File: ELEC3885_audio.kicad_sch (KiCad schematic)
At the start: 27 parts, among them U2 SGTL5000XNLA3, U3 AP7313

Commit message: Schematic work
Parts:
- removed J?: LineOutL, symbol Connector:AudioJack2
- removed J?: LineOutR, symbol Connector:AudioJack2
- removed J?: LineIn, symbol Connector:AudioJack3
- removed L1: Ferrite 600, symbol Device:L
- added C7: 1uF, Capacitor_SMD:C_0402_1005Metric, symbol Device:C_Small
- added FB1: FerriteBead, Inductor_SMD:L_0603_1608Metric, symbol Device:FerriteBead
- added J2: LineIn, Connector_Audio:Jack_3.5mm_CUI_SJ1-3535NG_Horizontal, symbol Connector:AudioJack3_SwitchTR
- added J4: LineOutR, Connector_Audio:Jack_6.35mm_Neutrik_NMJ4HCD2_Horizontal, symbol Connector:AudioJack2_SwitchT
- added J5: LineOutL, Connector_Audio:Jack_6.35mm_Neutrik_NMJ4HCD2_Horizontal, symbol Connector:AudioJack2_SwitchT
- C1: renamed from C11; value 2.2uF -> 10uF; footprint (none) -> Capacitor_SMD:C_0603_1608Metric
- C10: renamed from C8; value 0.1uF -> 1uF; footprint (none) -> Capacitor_SMD:C_0402_1005Metric
- C11: renamed from C3; footprint (none) -> Capacitor_SMD:C_0603_1608Metric
- C12: renamed from C4; footprint (none) -> Capacitor_SMD:C_0603_1608Metric
- C13: renamed from C?; footprint (none) -> Capacitor_SMD:C_0603_1608Metric
- C14: renamed from C?; footprint (none) -> Capacitor_SMD:C_0402_1005Metric
- C2: renamed from C10; footprint (none) -> Capacitor_SMD:C_0402_1005Metric
- C3: renamed from C9; footprint (none) -> Capacitor_SMD:C_0402_1005Metric
- C4: renamed from C1; footprint (none) -> Capacitor_SMD:C_0603_1608Metric
- C5: renamed from C2; footprint (none) -> Capacitor_SMD:C_0603_1608Metric
- C6: renamed from C5; value 0.15uF -> 0.1uF; footprint (none) -> Capacitor_SMD:C_0402_1005Metric
- C8: renamed from C6; value 2.2uF -> 0.1uF; footprint (none) -> Capacitor_SMD:C_0402_1005Metric
- C9: renamed from C7; value 2.2uF -> 10nF; footprint (none) -> Capacitor_SMD:C_0402_1005Metric
- J1: renamed from J?; footprint (none) -> Connector_Audio:Jack_XLR_Neutrik_NC3FAAH-0_Horizontal
- J3: renamed from J?; footprint (none) -> Connector_Audio:Jack_3.5mm_CUI_SJ-3523-SMT_Horizontal
- MK1: renamed from MK?; footprint (none) -> Connector_PinSocket_2.54mm:PinSocket_1x02_P2.54mm_Vertical
- R1, R2, R3: footprint (none) -> Resistor_SMD:R_0402_1005Metric
- R4: renamed from R?; footprint (none) -> Resistor_SMD:R_0402_1005Metric
- RV1: renamed from RV?; footprint (none) -> Potentiometer_THT:Potentiometer_Alpha_RD901F-40-00D_Single_Vertical
- U1: renamed from U3; footprint (none) -> LukeLibrary:SOT23
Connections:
- net AGND is gone; now on net GND: RV1.1
- net +3.3V: now also C7.1, FB1.1
- net GND: now also C7.2, J2.RN, J2.S, J2.TN, J4.S, J4.TN, J5.S, J5.TN
- net LINE_IN_L: now also J2.R
- net LINE_IN_R: now also J2.T
- net LINE_OUT_L: now also J5.T
- net LINE_OUT_R: now also J4.T
- net at C10.1, C9.1, U2.3 (VDDA): now also FB1.2
- net VOLUME_IN renamed VOLUME_CONTROL
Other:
- note added: "Analogue Filtering"
- note added: "Codec"
- note added: "Decoupling"
- note added: "I/O"
- note added: "Internal Mic"
- note added: "Mic Input"
- note added: "Volume Control"
- moved on the sheet: C1, C10, C11, C12, C13, C14, C2, C3, C4, C5, C6, C8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

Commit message: Initial schematic complete
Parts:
- added J8: Conn_01x06_Female, Connector_PinSocket_2.54mm:PinSocket_1x06_P2.54mm_Vertical, symbol Connector:Conn_01x06_Female
- added J9: Conn_01x05_Female, Connector_PinSocket_2.54mm:PinSocket_1x05_P2.54mm_Vertical, symbol Connector:Conn_01x05_Female
- J1: symbol Connector:XLR3_AudioJack3_Combo_Ground -> Connector:XLR3
- MK1: symbol Device:Microphone -> Connector:Conn_01x02_Female
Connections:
- net +3.3V: now also J9.5 (Pin_5)
- net GND: now also J1.1, J8.2 (Pin_2), J8.4 (Pin_4), J8.5 (Pin_5), J9.3 (Pin_3); no longer J1.G, J2.RN, J2.TN
- net MIC_IN: now also J8.6 (Pin_6)
- net at J1.2: now also J8.1 (Pin_1)
- net at J1.3: now also J8.3 (Pin_3)
- new net MEMS_IN: J2.RN, J2.TN, J9.2 (Pin_2)
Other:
- note added: "ECM Test Header"
- note added: "MEMS Test Header"
- moved on the sheet: C13, C14, MK1, R1, R4

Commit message: New Revision
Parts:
- MK1: symbol Connector:Conn_01x02_Female -> Device:Microphone
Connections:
- net GND: now also J1.3; no longer J1.1
- net at J8.3 (Pin_3): now also J1.1; no longer J1.3
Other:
- note removed: "ECM Test Header"
- note removed: "MEMS Test Header"
- moved on the sheet: MK1, R1

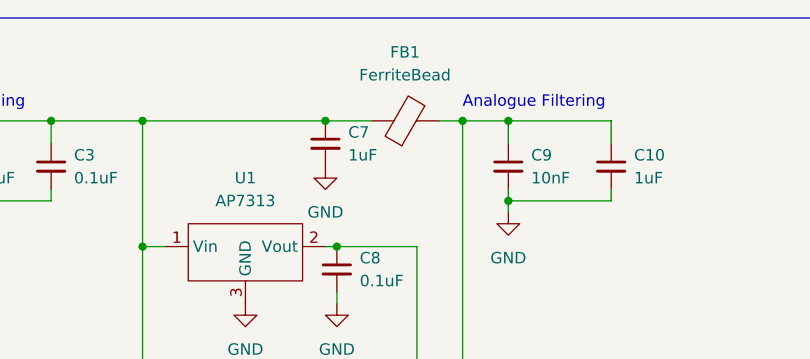
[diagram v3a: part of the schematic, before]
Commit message: Fab cleanup, trace tapers added
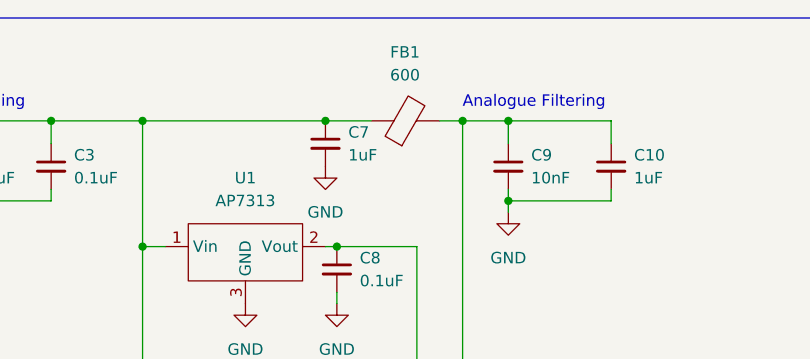
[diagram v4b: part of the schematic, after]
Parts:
- FB1: value FerriteBead -> 600
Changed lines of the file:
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@@
     (in_bom yes) (on_board yes) (fields_autoplaced)
     (property "Reference" "FB1" (id 0) (at 105.3592 17.78 90))
-    (property "Value" "FerriteBead" (id 1) (at 105.3592 20.32 90))
+    (property "Value" "600" (id 1) (at 105.3592 20.32 90))
     (property "Footprint" "Inductor_SMD:L_0603_1608Metric" (id 2) (at 105.41 27.178 90)
       (effects (font (size 1.27 1.27)) hide)

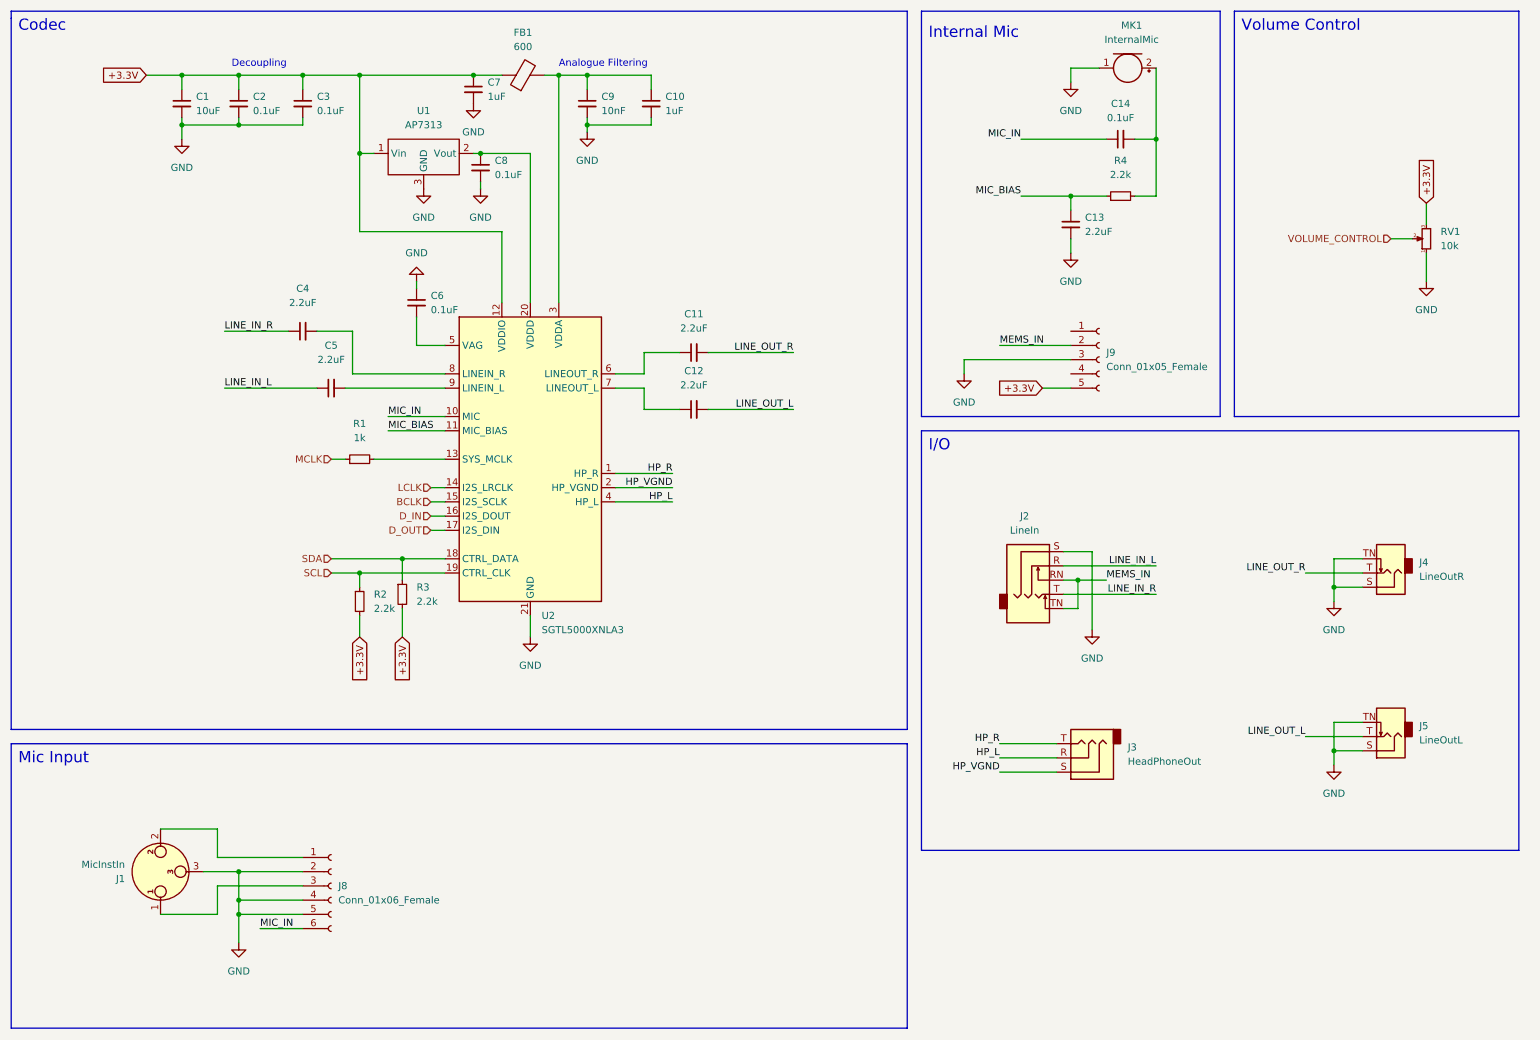
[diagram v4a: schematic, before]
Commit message: Moved to Rev 3, button + LED ui added
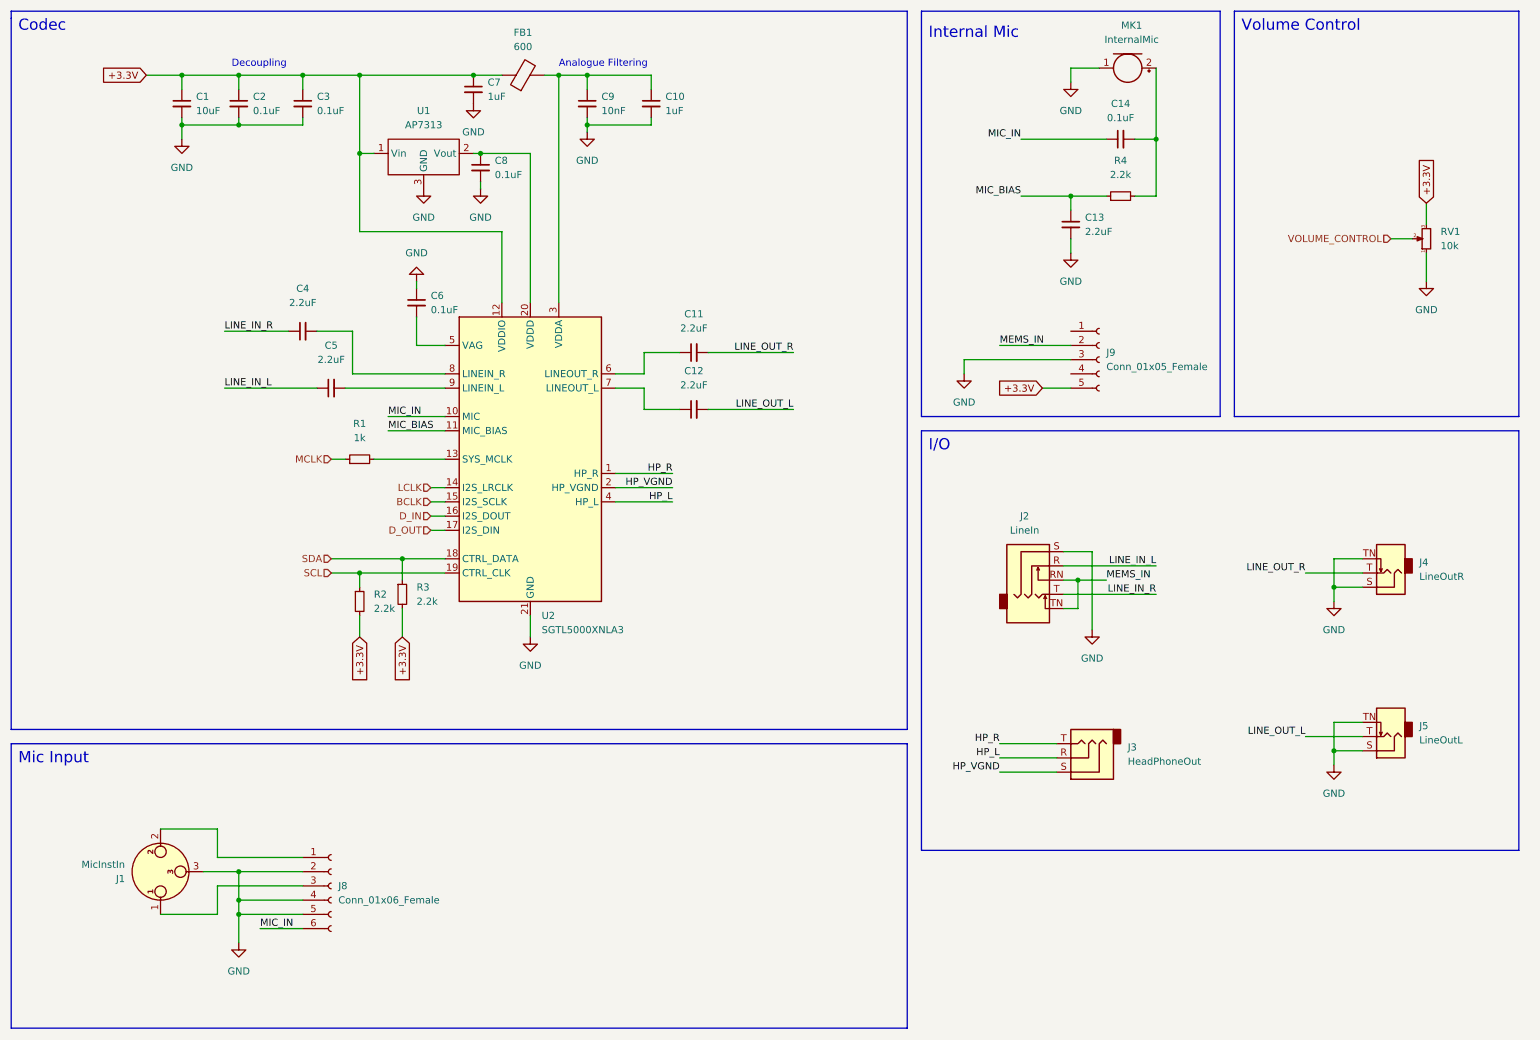
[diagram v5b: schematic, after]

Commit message: Rev3 PCB layout started
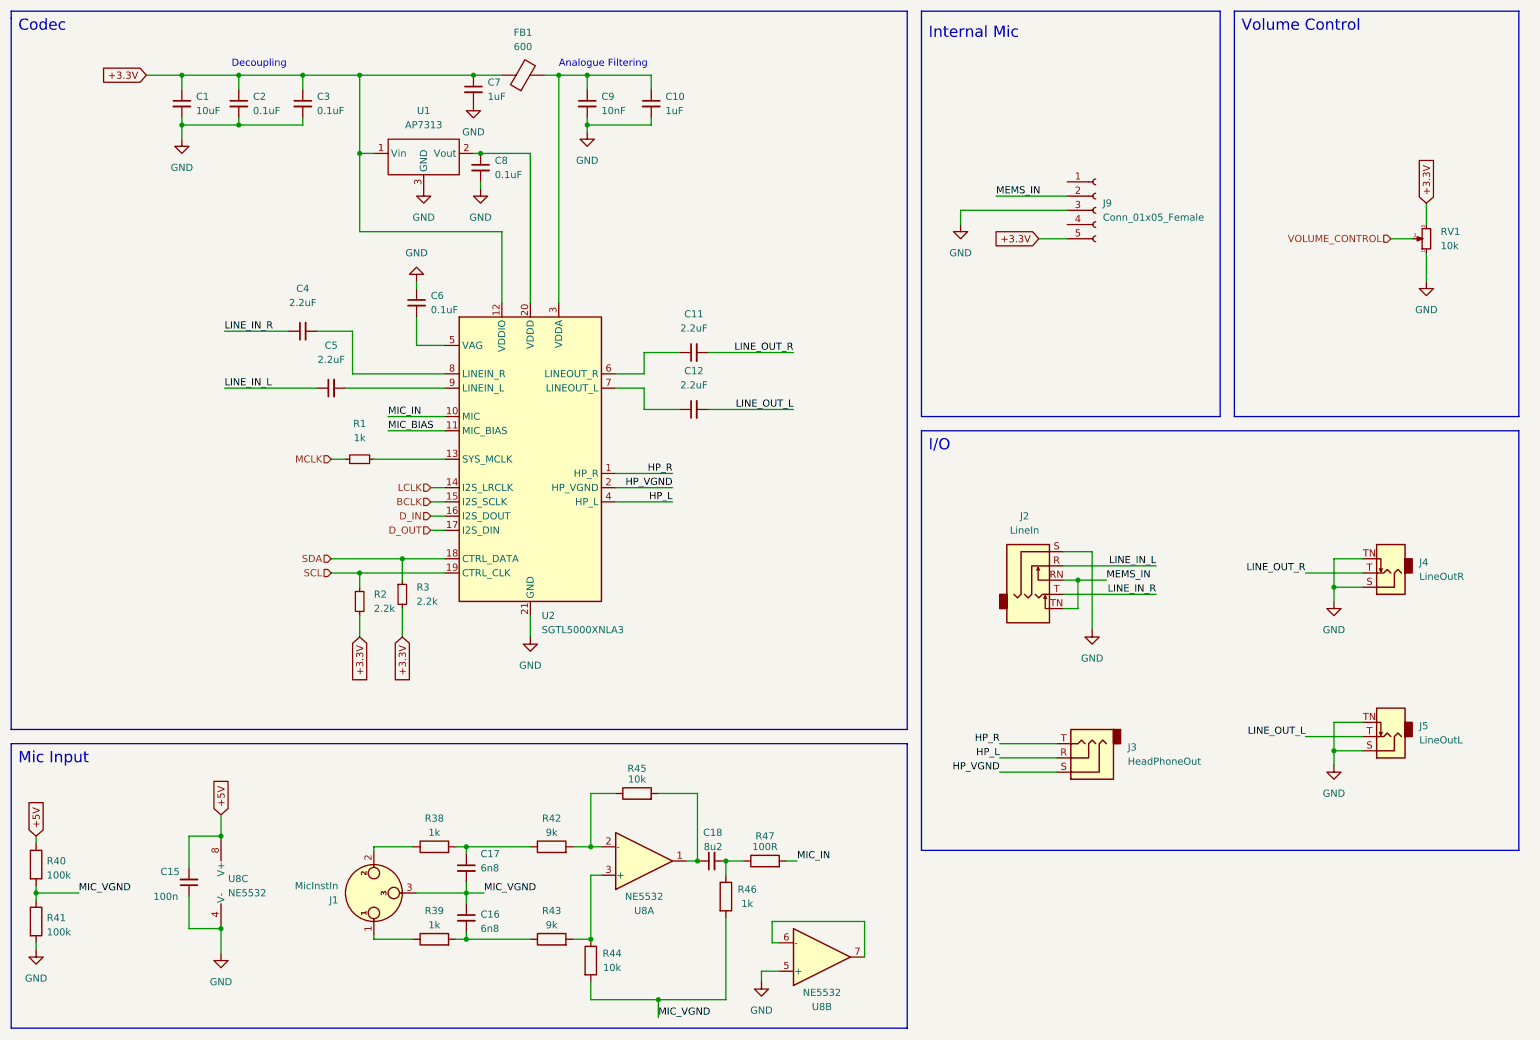
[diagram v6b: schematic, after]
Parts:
- removed C13: 2.2uF, Capacitor_SMD:C_0603_1608Metric, symbol Device:C_Small
- removed C14: 0.1uF, Capacitor_SMD:C_0402_1005Metric, symbol Device:C_Small
- removed J8: Conn_01x06_Female, Connector_PinSocket_2.54mm:PinSocket_1x06_P2.54mm_Vertical, symbol Connector:Conn_01x06_Female
- removed MK1: InternalMic, Connector_PinSocket_2.54mm:PinSocket_1x02_P2.54mm_Vertical, symbol Device:Microphone
- removed R4: 2.2k, Resistor_SMD:R_0402_1005Metric, symbol Device:R_Small
- added C15: 100n, symbol Device:C_Small
- added C16, C17: 6n8, symbol Device:C_Small
- added C18: 8u2, symbol Device:C_Small
- added R38, R39, R46: 1k, symbol Device:R
- added R40, R41: 100k, symbol Device:R
- added R42, R43: 9k, symbol Device:R
- added R44, R45: 10k, symbol Device:R
- added R47: 100R, symbol Device:R
- added U8: NE5532, symbol Amplifier_Operational:NE5532
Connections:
- net GND: now also C15.1, R41.2, U8.4 (V-), U8.5 (+); no longer J1.3
- net MIC_IN: now also R47.2
- net at J1.1: now also R39.1
- net at J1.2: now also R38.1
- new net: C16.2, R39.2, R43.1
- new net: R43.2, R44.1, U8.3 (+)
- new net: C17.1, R38.2, R42.1
- new net: C18.2, R46.1, R47.1
- new net: R42.2, R45.1, U8.2 (-)
- new net: C18.1, R45.2, U8.1
- new net: U8.6 (-), U8.7
- new net +5V: C15.2, R40.1, U8.8 (V+)
- new net MIC_VGND: C16.1, C17.2, J1.3, R40.2, R41.1, R44.2, R46.2
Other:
- moved on the sheet: J1, J9

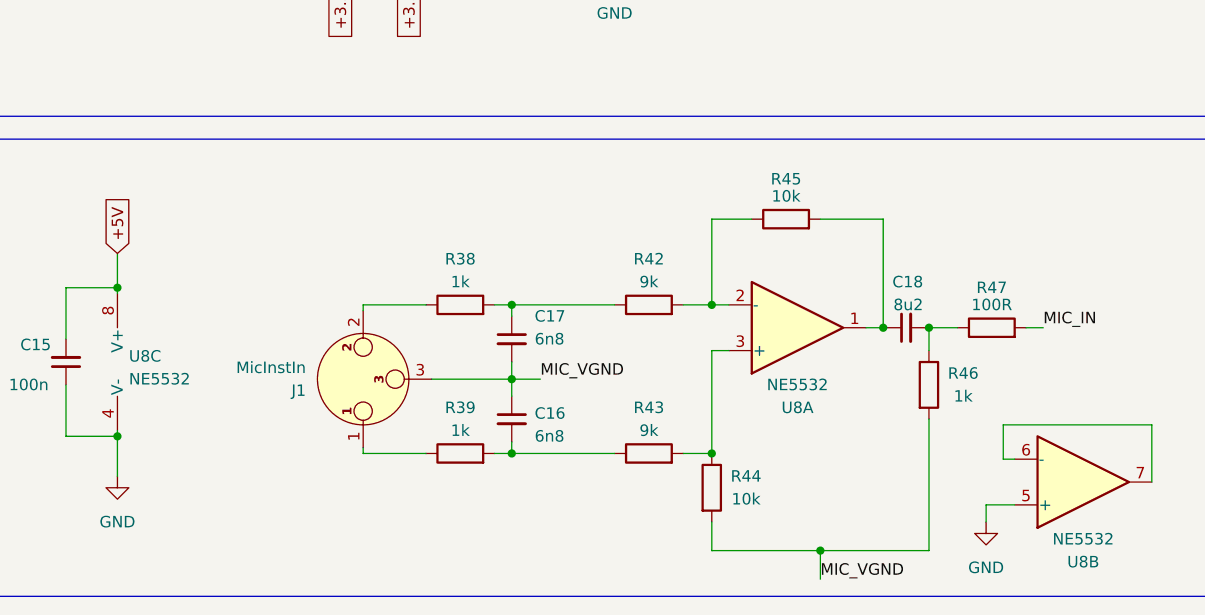
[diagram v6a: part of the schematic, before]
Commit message: Rev3 rework, diff amp jumpers added
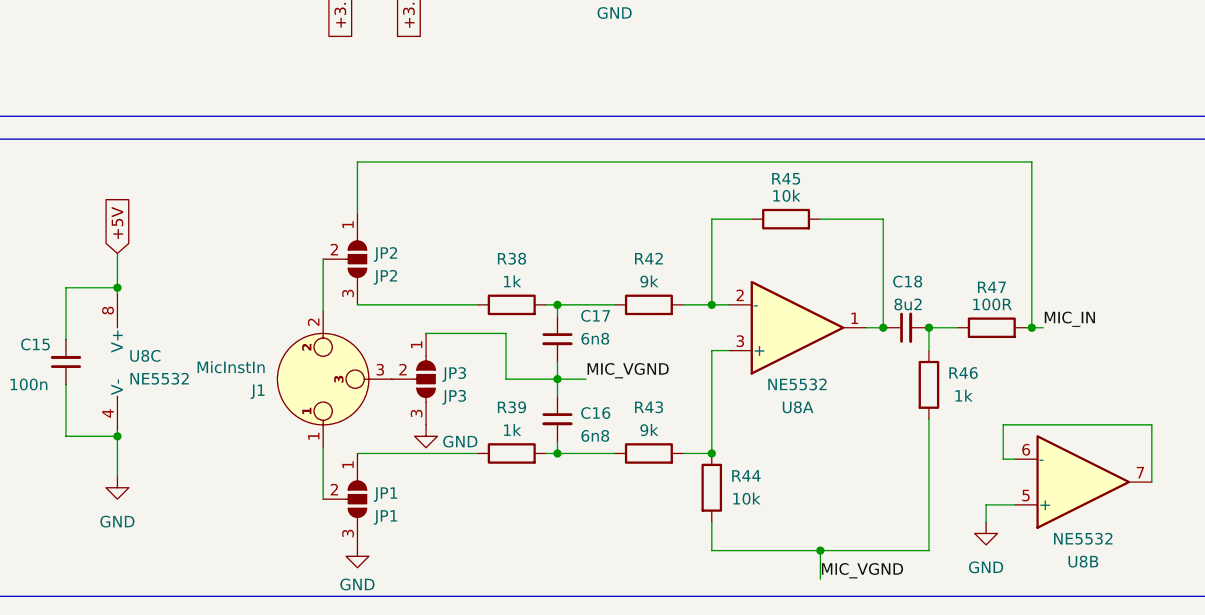
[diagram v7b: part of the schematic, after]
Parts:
- added JP1: JP1, Jumper:SolderJumper-3_P1.3mm_Open_RoundedPad1.0x1.5mm, symbol Jumper:SolderJumper_3_Open
- added JP2: JP2, Jumper:SolderJumper-3_P1.3mm_Open_RoundedPad1.0x1.5mm, symbol Jumper:SolderJumper_3_Open
- added JP3: JP3, Jumper:SolderJumper-3_P1.3mm_Open_RoundedPad1.0x1.5mm, symbol Jumper:SolderJumper_3_Open
- C15, C16, C17, C18: footprint (none) -> Capacitor_SMD:C_0402_1005Metric
- R38, R39, R46, R47: footprint (none) -> Resistor_SMD:R_0402_1005Metric
- R40, R41, R42, R43, R44, R45: footprint (none) -> Resistor_SMD:R_0603_1608Metric
- U8: footprint (none) -> Package_SO:SOIC-8-1EP_3.9x4.9mm_P1.27mm_EP2.29x3mm
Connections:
- net GND: now also JP1.3 (B), JP3.3 (B)
- net MIC_IN: now also JP2.1 (A)
- net MIC_VGND: now also JP3.1 (A); no longer J1.3
- net at J1.1: now also JP1.2 (C); no longer R39.1
- net at J1.2: now also JP2.2 (C); no longer R38.1
- new net: J1.3, JP3.2 (C)
- new net: JP2.3 (B), R38.1
- new net: JP1.1 (A), R39.1
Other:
- moved on the sheet: C16, C17, J1, R38, R39
